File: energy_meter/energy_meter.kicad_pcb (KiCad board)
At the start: 2 copper layers, 123 parts, among them IC1 ADUM4151BRIZ, IC2 ADUM6404ARIZ, IC3 ADP122AUJZ-3.3-R7, J1 Screw_Terminal_01x02, J2 Screw_Terminal_01x02, T1 T60404-E4626-X502, T2 T60404-E4626-X502, U1 ADE9000ACPZ, U2 SN74LV4T125PWR, U3 SN74LV4T125PWR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

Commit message: Finish up schematic
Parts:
- added C36: 1u, Capacitor_SMD:C_0805_2012Metric_Pad1.18x1.45mm_HandSolder, F.Cu at (100.6, 68.1)
- added C37: 4.7u, Capacitor_SMD:C_0805_2012Metric_Pad1.18x1.45mm_HandSolder, F.Cu at (94.2, 83.3)
- added C38: 0.1u, Capacitor_SMD:C_0805_2012Metric_Pad1.18x1.45mm_HandSolder, F.Cu at (94.2, 86.4)
- added C39: 0.1u, Capacitor_SMD:C_0805_2012Metric_Pad1.18x1.45mm_HandSolder, F.Cu at (136.4, 32.1)
- added C40: 10u, Capacitor_SMD:C_0805_2012Metric_Pad1.18x1.45mm_HandSolder, F.Cu at (136.4, 35.1)
- added C41: 0.1u, Capacitor_SMD:C_0805_2012Metric_Pad1.18x1.45mm_HandSolder, F.Cu at (136.4, 38.1)
- added C42: 10u, Capacitor_SMD:C_0805_2012Metric_Pad1.18x1.45mm_HandSolder, F.Cu at (136.4, 41.1)
- added C43: 22u, Capacitor_SMD:C_0805_2012Metric_Pad1.18x1.45mm_HandSolder, F.Cu at (136.4, 44.1)
- added C44: 0.1u, Capacitor_SMD:C_0805_2012Metric_Pad1.18x1.45mm_HandSolder, F.Cu at (136.4, 47.1)
- added D6: D_Schottky, Diode_SMD:D_SOD-323_HandSoldering, F.Cu at (95.7, 68.1)
- added D7: D_Schottky, Diode_SMD:D_SOD-323_HandSoldering, F.Cu at (95.7, 71.1)
- added D8: D_Schottky, Diode_SMD:D_SOD-323_HandSoldering, F.Cu at (141.3, 58.7)
- added IC4: 24LC32A_SN, 24LC32A_SN:SOIC127P600X175-8N, F.Cu at (96.0, 78.6)
- added J3: ZX62-AB-5PA_31_, microUSB:ZX62AB5PA31, F.Cu at (139.9, 53.0)
- added R30: 10k, Resistor_SMD:R_0805_2012Metric_Pad1.20x1.40mm_HandSolder, F.Cu at (100.6, 71.1)
- added R31: 10k, Resistor_SMD:R_0805_2012Metric_Pad1.20x1.40mm_HandSolder, F.Cu at (136.3, 58.7)
- added R32: 10k, Resistor_SMD:R_0805_2012Metric_Pad1.20x1.40mm_HandSolder, F.Cu at (136.3, 61.7)
- added R33: 10k, Resistor_SMD:R_0805_2012Metric_Pad1.20x1.40mm_HandSolder, F.Cu at (136.3, 64.6)
- added SW1: SW_Push, Button_Switch_THT:SW_PUSH_6mm, F.Cu at (95.2, 60.1)
- added U4: Pico_SMD_NODEBUG, RPi Pico:RPi_PicoW_SMD, F.Cu at (121.9, 57.1)

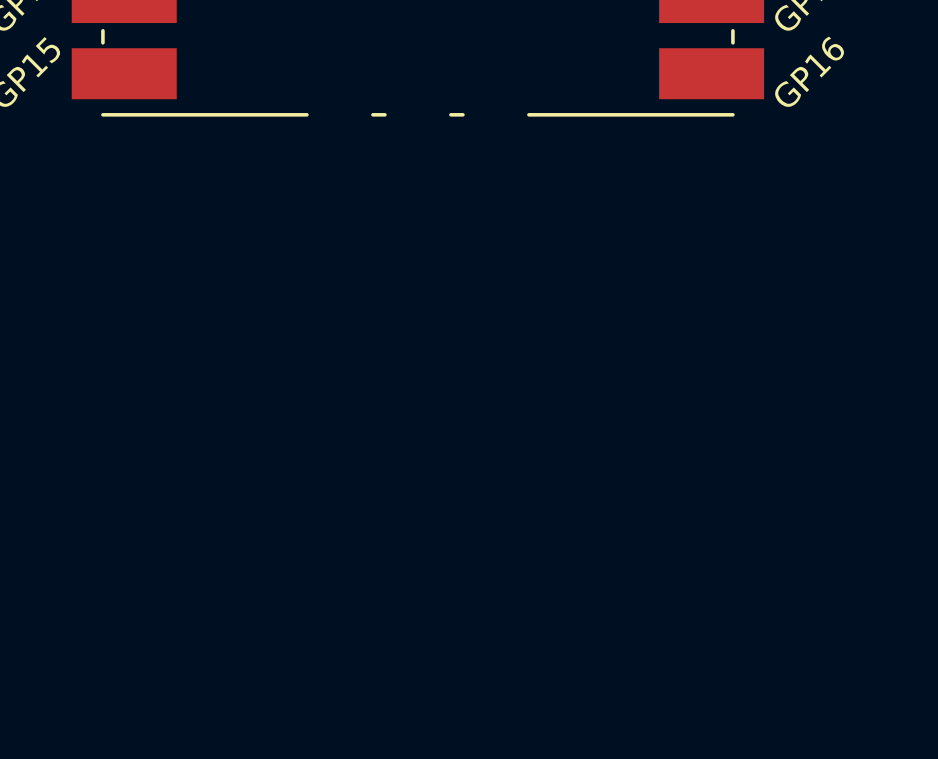
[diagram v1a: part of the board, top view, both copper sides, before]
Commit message: Add lipo battery terminal
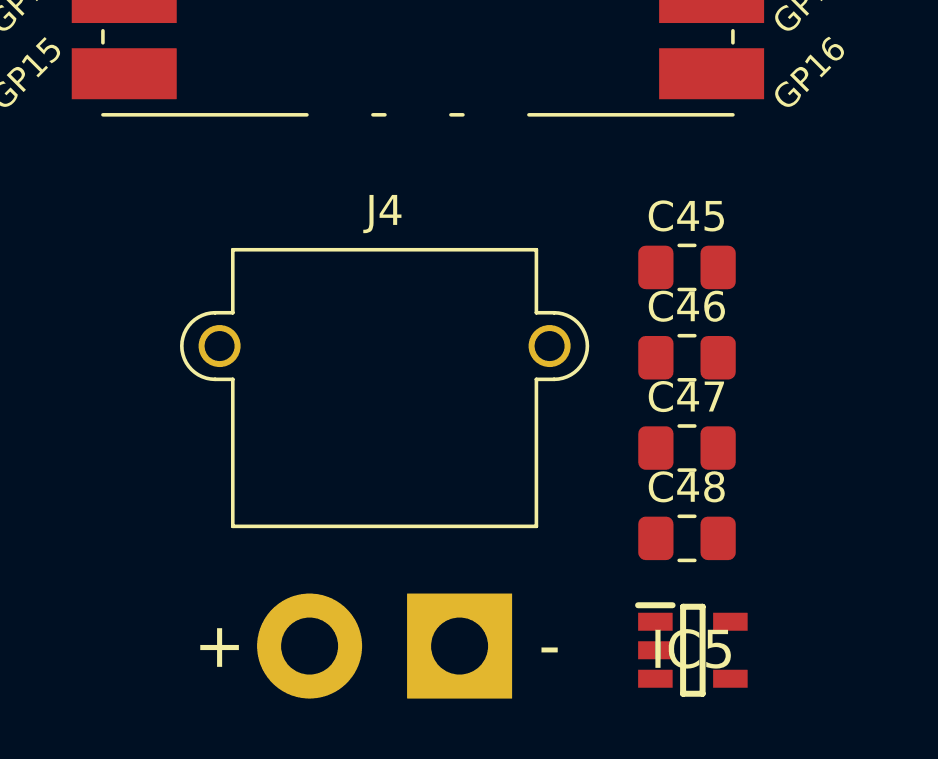
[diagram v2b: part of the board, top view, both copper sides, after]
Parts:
- added C45: 10u, Capacitor_SMD:C_0805_2012Metric_Pad1.18x1.45mm_HandSolder, F.Cu at (130.9, 87.7)
- added C46: 0.1u, Capacitor_SMD:C_0805_2012Metric_Pad1.18x1.45mm_HandSolder, F.Cu at (130.9, 90.7)
- added C47: 10u, Capacitor_SMD:C_0805_2012Metric_Pad1.18x1.45mm_HandSolder, F.Cu at (130.9, 93.8)
- added C48: 0.1u, Capacitor_SMD:C_0805_2012Metric_Pad1.18x1.45mm_HandSolder, F.Cu at (130.9, 96.8)
- added IC5: ADP122AUJZ-3.3-R7, ADP122AUJZ-3.3-R7:SOT95P280X100-5N, F.Cu at (131.1, 100.5)
- added J4: XT30, Connector_AMASS:AMASS_XT30PW-M_1x02_P2.50mm_Horizontal, F.Cu at (123.3, 100.4)
- J3: value ZX62-AB-5PA_31_ -> MicroUSB

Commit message: Minor changes
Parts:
- moved IC2 55.4 mm to (68.6, 102.0)
- moved U3 24.0 mm to (58.5, 101.6), turned to -90 degrees
- moved U2 21.7 mm to (78.7, 101.9), turned to 90 degrees
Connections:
- C23 pad 1: GNDA -> +5V_PICO
- C28 pad 2: GNDA -> +5V_PICO
- C29 pad 2: GNDA -> +5V_PICO
- C30 pad 1: GNDA -> +5V_PICO
- C31 pad 2: GNDA -> +5V_PICO
- C37 pad 2: GNDA -> +5V_PICO
- C38 pad 2: GNDA -> +5V_PICO
- C39 pad 2: GNDA -> +5V_PICO
- C40 pad 2: GNDA -> +5V_PICO
- C41 pad 2: GNDA -> +5V_PICO
- C42 pad 2: GNDA -> +5V_PICO
- C43 pad 2: GNDA -> +5V_PICO
- C44 pad 2: GNDA -> +5V_PICO
- D5 pad 1: IRQ0_ADE -> GND
- IC1 pad 10: GNDA -> +5V_PICO
- IC1 pad 2: GNDA -> +5V_PICO
- IC2 pad 10: +3V3_ADE -> +5V_ADE
- IC2 pad 2: GNDA -> +5V_PICO
- IC2 pad 8: GNDA -> +5V_PICO
- IC4 pad 1: GNDA -> +5V_PICO
- IC4 pad 2: GNDA -> +5V_PICO
- IC4 pad 3: GNDA -> +5V_PICO
- IC4 pad 4: GNDA -> +5V_PICO
- IC4 pad 7: GNDA -> +5V_PICO
- J3 pad 5: GNDA -> +5V_PICO
- J3 pad MP1: GNDA -> +5V_PICO
- J3 pad MP2: GNDA -> +5V_PICO
- J3 pad MP3: GNDA -> +5V_PICO
- J3 pad MP4: GNDA -> +5V_PICO
- J3 pad MP5: GNDA -> +5V_PICO
- J3 pad MP6: GNDA -> +5V_PICO
- J4 pad 1: GNDA -> +5V_PICO
- R29 pad 1: GNDA -> +5V_PICO
- SW1 pad 1: GNDA -> +5V_PICO
- TP31 pad 1: GNDA -> +5V_PICO
- TP32 pad 1: GNDA -> +5V_PICO
- U3 pad 1: GNDA -> +5V_PICO
- U3 pad 10: GNDA -> +5V_PICO
- U3 pad 13: GNDA -> +5V_PICO
- U3 pad 4: GNDA -> +5V_PICO
- U3 pad 7: GNDA -> +5V_PICO
- U4 pad 13: GNDA -> +5V_PICO
- U4 pad 18: GNDA -> +5V_PICO
- U4 pad 23: GNDA -> +5V_PICO
- U4 pad 28: GNDA -> +5V_PICO
- U4 pad 3: GNDA -> +5V_PICO
- U4 pad 33: GNDA -> +5V_PICO
- U4 pad 38: GNDA -> +5V_PICO
- U4 pad 8: GNDA -> +5V_PICO

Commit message: Minor changes
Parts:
- added J5: VA, Connector:Banana_Cliff_FCR7350R_S16N-PC_Horizontal, F.Cu at (158.0, 35.6)
- added J6: VB, Connector:Banana_Cliff_FCR7350R_S16N-PC_Horizontal, F.Cu at (172.0, 35.6)
- added J7: EARTH, Connector:Banana_Cliff_FCR7350B_S16N-PC_Horizontal, F.Cu at (186.1, 35.6)
- added U5: BME280, BME280_beakout:BME_breakout, F.Cu at (102.2, 100.1)
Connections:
- C23 pad 1: +5V_PICO -> GNDA
- C28 pad 2: +5V_PICO -> GNDA
- C29 pad 2: +5V_PICO -> GNDA
- C30 pad 1: +5V_PICO -> GNDA
- C30 pad 2: Net-(IC2-VDDL) -> +5V_PICO
- C31 pad 2: +5V_PICO -> GNDA
- C37 pad 2: +5V_PICO -> GNDA
- C38 pad 2: +5V_PICO -> GNDA
- C39 pad 2: +5V_PICO -> GNDA
- C40 pad 2: +5V_PICO -> GNDA
- C41 pad 2: +5V_PICO -> GNDA
- C42 pad 2: +5V_PICO -> GNDA
- C43 pad 2: +5V_PICO -> GNDA
- C44 pad 2: +5V_PICO -> GNDA
- IC1 pad 10: +5V_PICO -> GNDA
- IC1 pad 2: +5V_PICO -> GNDA
- IC2 pad 2: +5V_PICO -> GNDA
- IC2 pad 7: Net-(IC2-VDDL) -> +5V_PICO
- IC2 pad 8: +5V_PICO -> GNDA
- IC4 pad 1: +5V_PICO -> GNDA
- IC4 pad 2: +5V_PICO -> GNDA
- IC4 pad 3: +5V_PICO -> GNDA
- IC4 pad 4: +5V_PICO -> GNDA
- IC4 pad 7: +5V_PICO -> GNDA
- J3 pad 5: +5V_PICO -> GNDA
- J3 pad MP1: +5V_PICO -> GNDA
- J3 pad MP2: +5V_PICO -> GNDA
- J3 pad MP3: +5V_PICO -> GNDA
- J3 pad MP4: +5V_PICO -> GNDA
- J3 pad MP5: +5V_PICO -> GNDA
- J3 pad MP6: +5V_PICO -> GNDA
- J4 pad 1: +5V_PICO -> GNDA
- R29 pad 1: +5V_PICO -> GNDA
- SW1 pad 1: +5V_PICO -> GNDA
- TP31 pad 1: +5V_PICO -> GNDA
- TP32 pad 1: +5V_PICO -> GNDA
- U2 pad 11: Net-(IC2-VIB) -> Net-(IC2-VID)
- U2 pad 12: IRQ1_ADE -> DREADY_ADE
- U2 pad 2: ZX_ADE -> IRQ0_ADE
- U2 pad 3: Net-(IC2-VIC) -> Net-(IC2-VIA)
- U2 pad 5: DREADY_ADE -> IRQ1_ADE
- U2 pad 6: Net-(IC2-VID) -> Net-(IC2-VIB)
- U2 pad 8: Net-(IC2-VIA) -> Net-(IC2-VIC)
- U2 pad 9: IRQ0_ADE -> ZX_ADE
- U3 pad 1: +5V_PICO -> GNDA
- U3 pad 10: +5V_PICO -> GNDA
- U3 pad 13: +5V_PICO -> GNDA
- U3 pad 4: +5V_PICO -> GNDA
- U3 pad 7: +5V_PICO -> GNDA
- U4 pad 13: +5V_PICO -> GNDA
- U4 pad 18: +5V_PICO -> GNDA
- U4 pad 23: +5V_PICO -> GNDA
- U4 pad 28: +5V_PICO -> GNDA
- U4 pad 3: +5V_PICO -> GNDA
- U4 pad 33: +5V_PICO -> GNDA
- U4 pad 38: +5V_PICO -> GNDA
- U4 pad 8: +5V_PICO -> GNDA

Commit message: finish schematic started on layout
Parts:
- added BZ1: Buzzer, Buzzer_Beeper:Buzzer_12x9.5RM7.6, F.Cu at (-46.2, 81.0)
- added C49: 0.1u, Capacitor_SMD:C_0805_2012Metric_Pad1.18x1.45mm_HandSolder, F.Cu at (-27.3, 83.1)
- added C50: 22u, Capacitor_SMD:C_0805_2012Metric_Pad1.18x1.45mm_HandSolder, F.Cu at (-27.3, 86.1)
- added J10: EARTH, TerminalBlock_Phoenix:TerminalBlock_Phoenix_MKDS-1,5-2_1x02_P5.00mm_Horizontal, F.Cu at (48.0, 76.2)
- added J8: 5V_SMPS, TerminalBlock_Phoenix:TerminalBlock_Phoenix_MKDS-1,5-2_1x02_P5.00mm_Horizontal, F.Cu at (-45.6, 94.0)
- added J9: IA_in, TerminalBlock_Phoenix:TerminalBlock_Phoenix_MKDS-1,5-2_1x02_P5.00mm_Horizontal, F.Cu at (48.0, 36.9)
- added Q1: Q_NMOS_SGD, Package_TO_SOT_SMD:SOT-23, F.Cu at (-55.8, 92.8)
- added R34: 10k, Resistor_SMD:R_0805_2012Metric_Pad1.20x1.40mm_HandSolder, F.Cu at (-60.6, 92.0)
- added R35: 1k, Resistor_SMD:R_0805_2012Metric_Pad1.20x1.40mm_HandSolder, F.Cu at (-60.6, 95.0)
- added U5: BME280, BME280_beakout:BME_breakout, F.Cu at (-55.4, 82.4)
- added U6: AMS1117-3.3, Package_TO_SOT_SMD:SOT-223-3_TabPin2, F.Cu at (-24.7, 77.5)
- C21: value 4.7u -> 10u
- T1: value T60404-E4626-X502 -> IA_in
- T2: value T60404-E4626-X502 -> IB_in
- moved C1 205.8 mm to (-159.4, 65.8)
- moved C10 205.8 mm to (-154.6, 71.8)
- moved C11 205.8 mm to (-154.6, 74.8)
- moved C12 205.8 mm to (-154.6, 77.8)
- moved C13 205.8 mm to (-154.6, 80.9)
- moved C14 205.8 mm to (-154.6, 83.9)
- moved C15 205.8 mm to (-149.7, 65.8)
- moved C16 205.8 mm to (-149.7, 68.8)
- moved C17 205.8 mm to (-149.7, 71.8)
- moved C18 205.8 mm to (-149.7, 74.8)
- moved C19 205.8 mm to (-149.7, 77.8)
- moved C2 205.8 mm to (-159.4, 68.8)
- moved C20 205.8 mm to (-149.7, 80.9)
- moved C21 205.8 mm to (-149.7, 83.9)
- moved C22 205.8 mm to (-144.9, 65.8)
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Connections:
- C20 pad 1: +3V3_ISO -> +3V3_ADE
- C21 pad 1: +3V3_ISO -> +3V3_ADE
- D8 pad 2: +3V3_ISO -> +5V_PICO
- U1 pad 1: +3V3_ISO -> +3V3_ADE
- U4 pad 20: unconnected-(U4-GPIO15-Pad20) -> BUZZER
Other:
- board outline added: 138.4 x 168.9 mm

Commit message: new
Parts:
- moved C5 243.0 mm to (78.6, 127.0), turned to 90 degrees
- moved C2 241.1 mm to (78.7, 106.7), turned to -90 degrees
- moved C4 240.9 mm to (74.9, 130.8), turned to -90 degrees
- moved C8 236.7 mm to (74.8, 124.2), turned to -90 degrees
- moved C3 233.7 mm to (71.1, 110.3), turned to -90 degrees
- moved C1 233.4 mm to (71.1, 102.8), turned to 90 degrees
- moved C10 223.6 mm to (68.9, 81.0), turned to 90 degrees
- moved C9 223.6 mm to (68.9, 75.9), turned to 90 degrees
- moved FB3 221.6 mm to (66.2, 138.4)
- moved FB2 218.6 mm to (66.2, 118.1)
- moved FB1 218.4 mm to (66.2, 113.0), turned to 180 degrees
- moved R9 216.9 mm to (64.8, 124.5), turned to 180 degrees
- moved R1 216.7 mm to (64.9, 106.7), turned to 180 degrees
- moved R14 214.3 mm to (64.8, 129.5)
- moved R4 211.1 mm to (64.8, 101.6)
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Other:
- board size 138.4 x 168.9 mm -> 138.4 x 137.2 mm

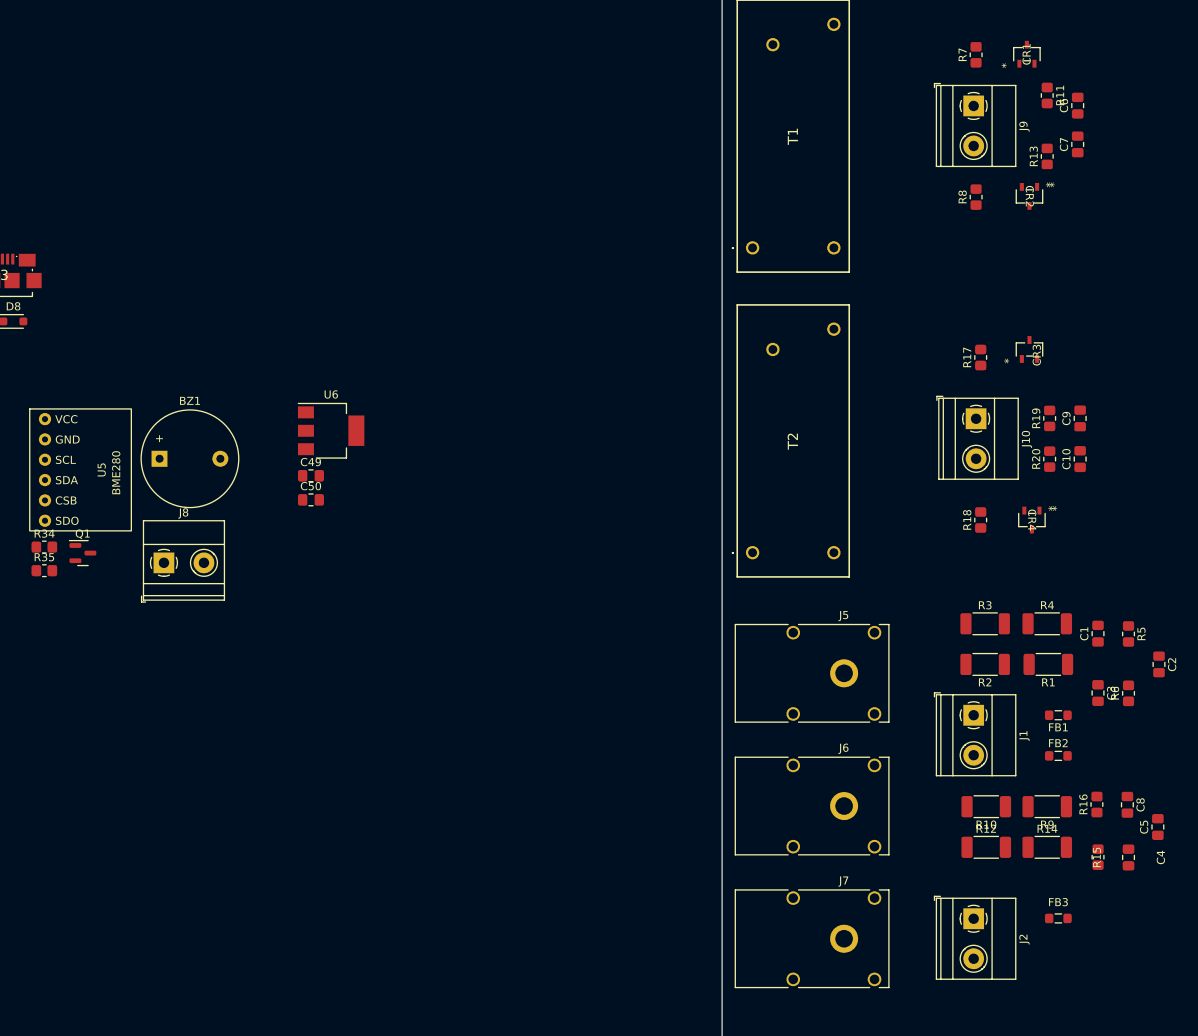
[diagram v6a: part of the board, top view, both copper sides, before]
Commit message: Remove banana cliffs
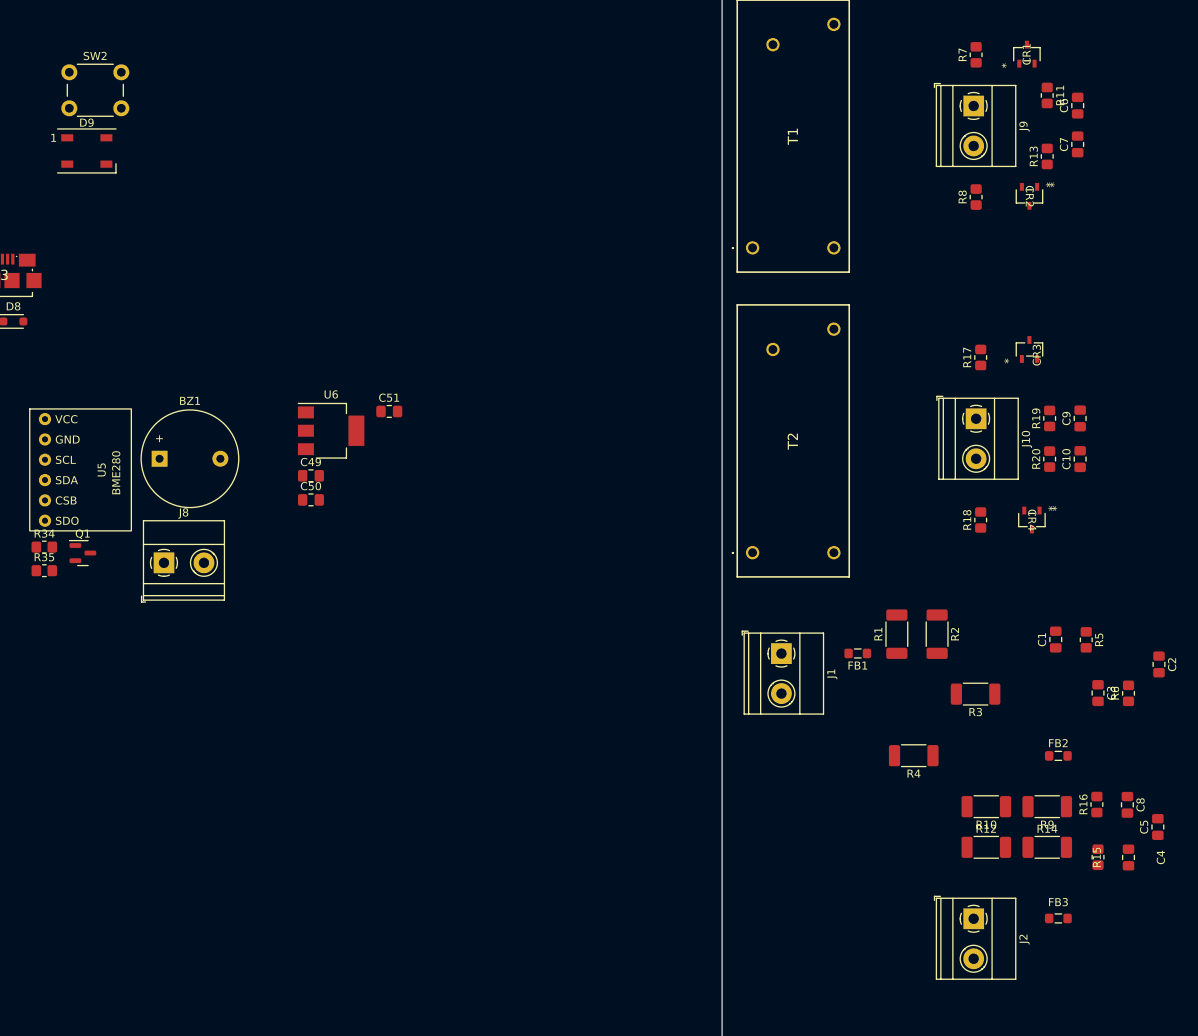
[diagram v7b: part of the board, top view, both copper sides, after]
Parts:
- removed J5: VA, Connector:Banana_Cliff_FCR7350R_S16N-PC_Horizontal
- removed J6: VB, Connector:Banana_Cliff_FCR7350R_S16N-PC_Horizontal
- removed J7: EARTH, Connector:Banana_Cliff_FCR7350B_S16N-PC_Horizontal
- added C51: 0.1u, Capacitor_SMD:C_0805_2012Metric_Pad1.18x1.45mm_HandSolder, F.Cu at (-17.5, 75.1)
- added D9: WS2812B, LED_SMD:LED_WS2812B_PLCC4_5.0x5.0mm_P3.2mm, F.Cu at (-55.3, 42.5)
- added SW2: SW_Push, Button_Switch_THT:SW_PUSH_6mm, F.Cu at (-57.5, 32.7)
- J10: value EARTH -> IB_in
- moved FB1 26.2 mm to (41.1, 105.3)
- moved J1 25.2 mm to (31.5, 105.3)
- moved R4 23.5 mm to (48.1, 118.1), turned to 180 degrees
- moved R1 19.3 mm to (46.0, 102.9), turned to 90 degrees
- moved R3 8.87 mm to (55.8, 110.4), turned to 180 degrees
- moved R2 7.10 mm to (51.0, 102.9), turned to -90 degrees
- moved C1 5.33 mm to (65.8, 103.6)
- moved R5 5.33 mm to (69.6, 103.6)
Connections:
- U4 pad 27: unconnected-(U4-GPIO21-Pad27) -> WS_LED
- U4 pad 34: unconnected-(U4-GPIO28_ADC2-Pad34) -> Net-(U4-GPIO28_ADC2)

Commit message: Basic layout
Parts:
- removed C45, C47: 10u, Capacitor_SMD:C_0805_2012Metric_Pad1.18x1.45mm_HandSolder
- removed C46, C48: 0.1u, Capacitor_SMD:C_0805_2012Metric_Pad1.18x1.45mm_HandSolder
- removed IC5: ADP122AUJZ-3.3-R7, ADP122AUJZ-3.3-R7:SOT95P280X100-5N
- removed J4: XT30, Connector_AMASS:AMASS_XT30PW-M_1x02_P2.50mm_Horizontal
- removed the U5 at (-103.5, 105.2)
- moved H4 279.0 mm to (139.1, 129.1)
- moved H3 271.1 mm to (139.1, 24.1)
- moved IC2 222.4 mm to (85.0, 96.6)
- moved IC1 206.0 mm to (85.0, 55.6)
- moved J3 205.6 mm to (139.8, 56.9), turned to 90 degrees
- moved U4 202.3 mm to (117.7, 79.6), turned to -90 degrees
- moved H2 199.8 mm to (49.1, 129.1)
- moved U5 195.6 mm to (137.8, 112.3)
- moved J8 189.9 mm to (138.5, 47.5), turned to 90 degrees
- moved H1 180.1 mm to (49.1, 24.1)
- moved J2 29.2 mm to (32.0, 121.3)
- moved FB3 27.1 mm to (41.9, 126.3)
- moved FB2 26.0 mm to (41.3, 110.3)
- moved R15 14.8 mm to (58.1, 123.6)
- moved C4 14.8 mm to (62.0, 123.6)
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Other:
- board size 138.4 x 137.2 mm -> 120 x 115 mm
